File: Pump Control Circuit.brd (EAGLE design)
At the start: 65.7 x 39 mm, 25 parts, among them IC1 317T, IC2 LM555N, J1 POWER_JACKPTH, K1 351, Q1 BC548, Q2 BC548

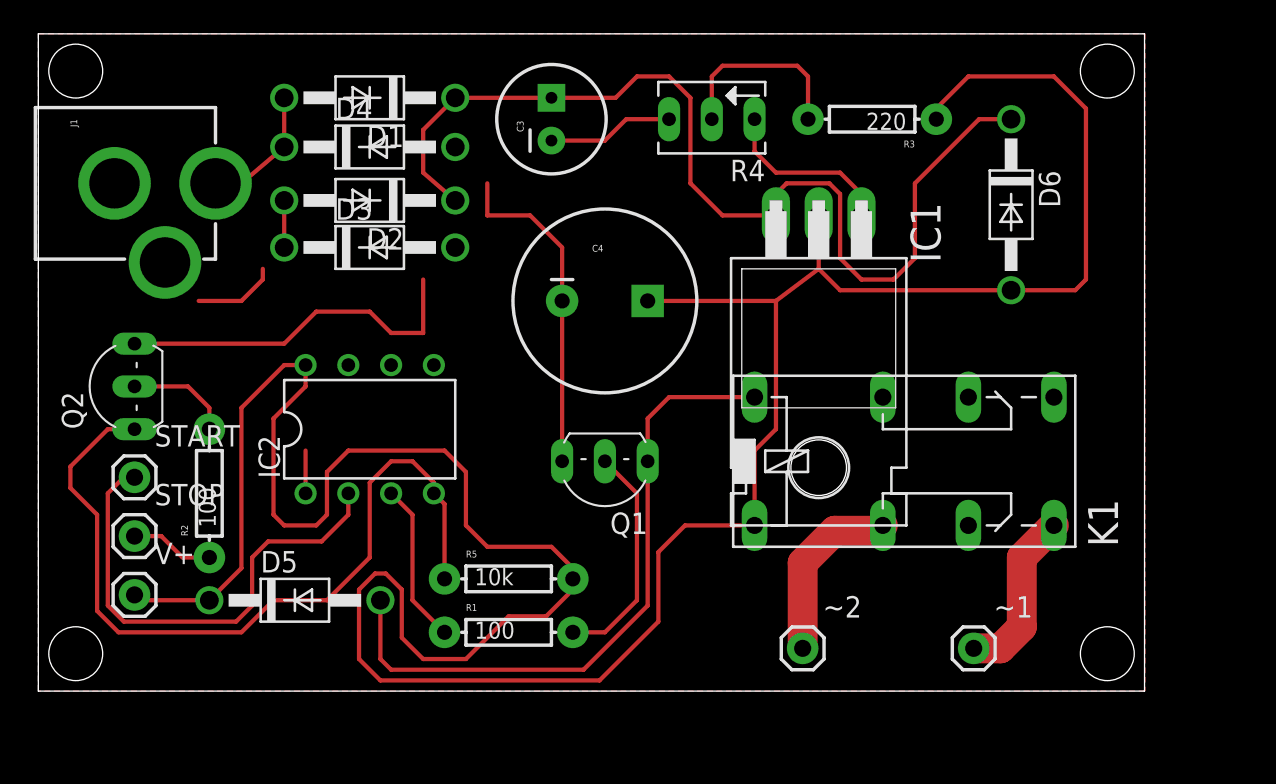
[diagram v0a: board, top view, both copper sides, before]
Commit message: Add files via upload
I changed the relay on the board schematic to allow for more options and to also allow for relay sizes I believe to be more commonly available in Rwanda.
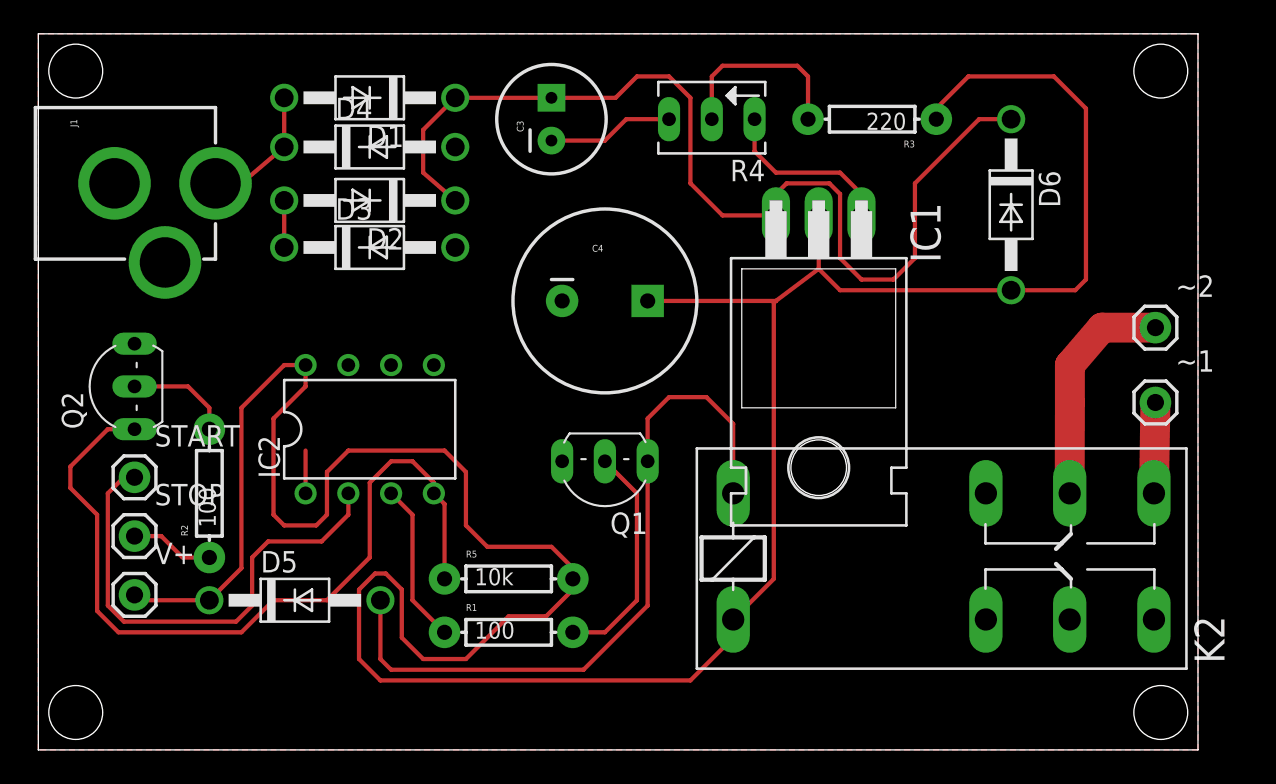
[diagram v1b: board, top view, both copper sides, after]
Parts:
- removed FRAME1: FRAME-LEDGER, SparkFun-Aesthetics:CREATIVE_COMMONS
- removed K1: 351, relay:351
- added K2: G2R2, relay:G2R2
- moved ~2 28.3 mm to (66.4, 62.5)
- moved ~1 18.2 mm to (66.4, 58.1)
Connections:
- removed net N$19: K1.P1, ~2.1
- new net N$9: K2.P1, ~2.1
- net N$13: now also K2.2; no longer K1.16
- net N$7: now also K2.S1; no longer K1.S1
- net V+: now also K2.1; no longer K1.1
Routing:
- net GND: track 59.3 -> 12.8 mm
- net N$9: track 0.00 -> 13.7 mm
- net N$19: track 10.8 -> 0.00 mm
- net N$7: track 10.2 -> 5.40 mm
- net N$13: track 39.2 -> 42.7 mm
- net V+: track 177.5 -> 178.2 mm
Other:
- board size 65.7 x 39 mm -> 68.9 x 42.5 mm

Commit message: Add files via upload
Fixed the voltage regulator footprint to not be intersecting with the relay footprint
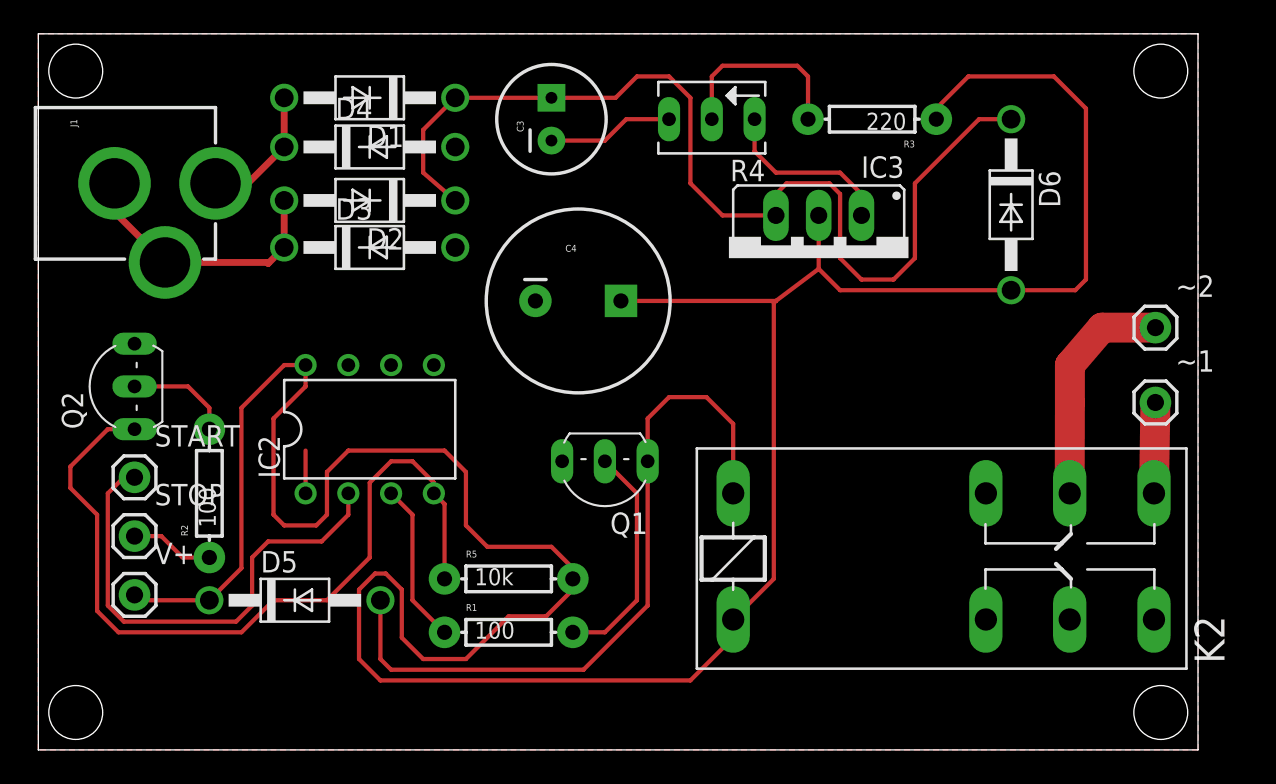
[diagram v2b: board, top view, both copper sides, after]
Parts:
- removed IC1: 317T, linear:TO220H
- added IC3: (no value), v-reg:317TS
- moved C4 1.59 mm to (32.1, 64.1)
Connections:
- new net NEUTRAL: D2.A, D3.C, J1.GND, J1.GNDBREAK
- net GND: no longer D2.A, D3.C, J1.GND, J1.GNDBREAK
- net N$1: now also IC3.1; no longer IC1.1
- net N$8: now also IC3.3; no longer IC1.3
- net V+: now also IC3.2; no longer IC1.2
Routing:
- net NEUTRAL: track 0.00 -> 16.2 mm
- net GND: track 12.8 -> 10.1 mm
- net V+: track 178.2 -> 179.8 mm
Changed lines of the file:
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@@
 <elements>
 <element name="C3" library="SparkFun-Capacitors" package="CPOL-RADIAL-100UF-25V" value="" x="30.48" y="74.93" rot="R90"/>
-<element name="C4" library="SparkFun-Capacitors" package="CPOL-RADIAL-1000UF-25V" value="" x="33.655" y="64.135"/>
+<element name="C4" library="SparkFun-Capacitors" package="CPOL-RADIAL-1000UF-25V" value="" x="32.0675" y="64.135"/>
 <element name="D1" library="diode" package="DO41-10" value="1N4004" x="19.685" y="76.2" rot="R180"/>
 <element name="D2" library="diode" package="DO41-10" value="1N4004" x="19.685" y="70.104" rot="R180"/>
@@
 <element name="D4" library="diode" package="DO41-10" value="1N4004" x="19.685" y="73.279"/>
 <element name="D5" library="diode" package="DO41-10" value="1N4004" x="15.24" y="46.355"/>
-<element name="IC1" library="linear" package="TO220H" value="317T" x="46.355" y="59.055" rot="R180"/>
 <element name="IC2" library="linear" package="DIL08" value="LM555N" x="19.685" y="56.515"/>
 <element name="J1" library="SparkFun-Connectors" package="POWER_JACK_PTH" value="POWER_JACKPTH" x="-3.175" y="71.12" rot="R270">
@@
 <attribute name="MF" value="OMRON COMPONENTS USA" x="43.815" y="48.895" size="1.778" layer="27" display="off"/>
 </element>
+<element name="IC3" library="v-reg" package="317TS" value="" x="46.355" y="66.675" rot="R180"/>
 </elements>
 <signals>
@@
 <contactref element="D4" pad="C"/>
 <contactref element="J1" pad="PWR"/>
-<wire x1="14.605" y1="76.2" x2="14.605" y2="73.279" width="0.254" layer="1"/>
-<wire x1="14.605" y1="73.279" x2="12.065" y2="71.12" width="0.254" layer="1"/>
-<wire x1="12.065" y1="71.12" x2="10.525" y2="71.12" width="0.254" layer="1"/>
+<wire x1="10.525" y1="71.12" x2="12.446" y2="71.12" width="0.4064" layer="1"/>
+<wire x1="12.446" y1="71.12" x2="14.605" y2="73.279" width="0.4064" layer="1"/>
+<wire x1="14.605" y1="73.279" x2="14.605" y2="76.2" width="0.4064" layer="1"/>
 </signal>
 <signal name="N$8">
 <contactref element="D1" pad="C"/>
 <contactref element="D2" pad="C"/>
-<contactref element="IC1" pad="3"/>
 <contactref element="C3" pad="1"/>
 <contactref element="D6" pad="C"/>
@@
 <wire x1="37.465" y1="77.47" x2="38.735" y2="76.2" width="0.254" layer="1"/>
 <wire x1="38.735" y1="76.2" x2="38.735" y2="71.12" width="0.254" layer="1"/>
-<wire x1="38.735" y1="71.12" x2="40.64" y2="69.215" width="0.254" layer="1"/>
-<wire x1="40.64" y1="69.215" x2="43.815" y2="69.215" width="0.254" layer="1"/>
 <wire x1="57.785" y1="74.93" x2="55.88" y2="74.93" width="0.254" layer="1"/>
 <wire x1="55.88" y1="74.93" x2="52.07" y2="71.12" width="0.254" layer="1"/>
@@
 <wire x1="47.625" y1="66.675" x2="47.625" y2="70.485" width="0.254" layer="1"/>
 <wire x1="47.625" y1="70.485" x2="46.99" y2="71.12" width="0.254" layer="1"/>
-<wire x1="46.99" y1="71.12" x2="44.45" y2="71.12" width="0.254" layer="1"/>
+<wire x1="44.45" y1="71.12" x2="46.99" y2="71.12" width="0.254" layer="1"/>
+<contactref element="IC3" pad="3"/>
 <wire x1="44.45" y1="71.12" x2="43.815" y2="70.485" width="0.254" layer="1"/>
 <wire x1="43.815" y1="70.485" x2="43.815" y2="69.215" width="0.254" layer="1"/>
+<wire x1="43.815" y1="69.215" x2="40.64" y2="69.215" width="0.254" layer="1"/>
+<wire x1="40.64" y1="69.215" x2="38.735" y2="71.12" width="0.254" layer="1"/>
 </signal>
 <signal name="GND">
@@
 <vertex x="0" y="37.465"/>
 </polygon>
-<contactref element="J1" pad="GNDBREAK"/>
-<contactref element="J1" pad="GND"/>
-<contactref element="D3" pad="C"/>
-<contactref element="D2" pad="A"/>
-<wire x1="14.605" y1="67.31" x2="14.605" y2="70.104" width="0.254" layer="1"/>
 </signal>
 <signal name="N$1">
-<contactref element="IC1" pad="1"/>
 <contactref element="R4" pad="E"/>
 <wire x1="42.545" y1="74.93" x2="42.545" y2="73.025" width="0.254" layer="1"/>
@@
 <wire x1="43.815" y1="71.755" x2="47.625" y2="71.755" width="0.254" layer="1"/>
 <wire x1="47.625" y1="71.755" x2="48.895" y2="70.485" width="0.254" layer="1"/>
+<contactref element="IC3" pad="1"/>
 <wire x1="48.895" y1="70.485" x2="48.895" y2="69.215" width="0.254" layer="1"/>
 </signal>
@@
 <signal name="V+">
 <contactref element="R3" pad="P$1"/>
-<contactref element="IC1" pad="2"/>
 <contactref element="C4" pad="+"/>
 <contactref element="IC2" pad="8"/>
@@
 <contactref element="D5" pad="C"/>
 <contactref element="D6" pad="A"/>
-<wire x1="36.195" y1="64.135" x2="43.815" y2="64.135" width="0.254" layer="1"/>
+<wire x1="34.6075" y1="64.135" x2="43.815" y2="64.135" width="0.254" layer="1"/>
 <wire x1="43.815" y1="64.135" x2="46.355" y2="66.04" width="0.254" layer="1"/>
-<wire x1="46.355" y1="69.215" x2="46.355" y2="66.04" width="0.254" layer="1"/>
 <wire x1="46.355" y1="66.04" x2="47.625" y2="64.77" width="0.254" layer="1"/>
 <wire x1="47.625" y1="64.77" x2="57.785" y2="64.77" width="0.254" layer="1"/>
@@
 <wire x1="43.688" y1="47.625" x2="43.688" y2="64.008" width="0.254" layer="1"/>
 <wire x1="43.688" y1="64.008" x2="43.815" y2="64.135" width="0.254" layer="1"/>
+<contactref element="IC3" pad="2"/>
+<wire x1="46.355" y1="66.04" x2="46.355" y2="69.215" width="0.254" layer="1"/>
 </signal>
 <signal name="N$2">
@@
 <wire x1="63.1825" y1="62.5475" x2="66.3575" y2="62.5475" width="1.778" layer="1"/>
 </signal>
+<signal name="NEUTRAL">
+<contactref element="J1" pad="GNDBREAK"/>
+<contactref element="J1" pad="GND"/>
+<contactref element="D3" pad="C"/>
+<contactref element="D2" pad="A"/>
+<wire x1="4.525" y1="71.12" x2="4.525" y2="69.42" width="0.4064" layer="1"/>
+<wire x1="4.525" y1="69.42" x2="7.525" y2="66.42" width="0.4064" layer="1"/>
+<wire x1="7.525" y1="66.42" x2="13.59" y2="66.42" width="0.4064" layer="1"/>
+<wire x1="13.59" y1="66.42" x2="13.6525" y2="66.3575" width="0.4064" layer="1"/>
+<wire x1="13.6525" y1="66.3575" x2="14.605" y2="67.31" width="0.4064" layer="1"/>
+<wire x1="14.605" y1="67.31" x2="14.605" y2="70.104" width="0.4064" layer="1"/>
+</signal>
 </signals>
